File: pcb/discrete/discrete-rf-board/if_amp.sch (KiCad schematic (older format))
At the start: 48 parts, among them Q401 NSVT65011MW6T1G, Q402 Q_NPN_BCE, Q403 NSVT65011MW6T1G, U401 NLAS4157DFT2G, U402 NLAS4157DFT2G, U403 NLAS4157DFT2G, U404 NLAS4157DFT2G

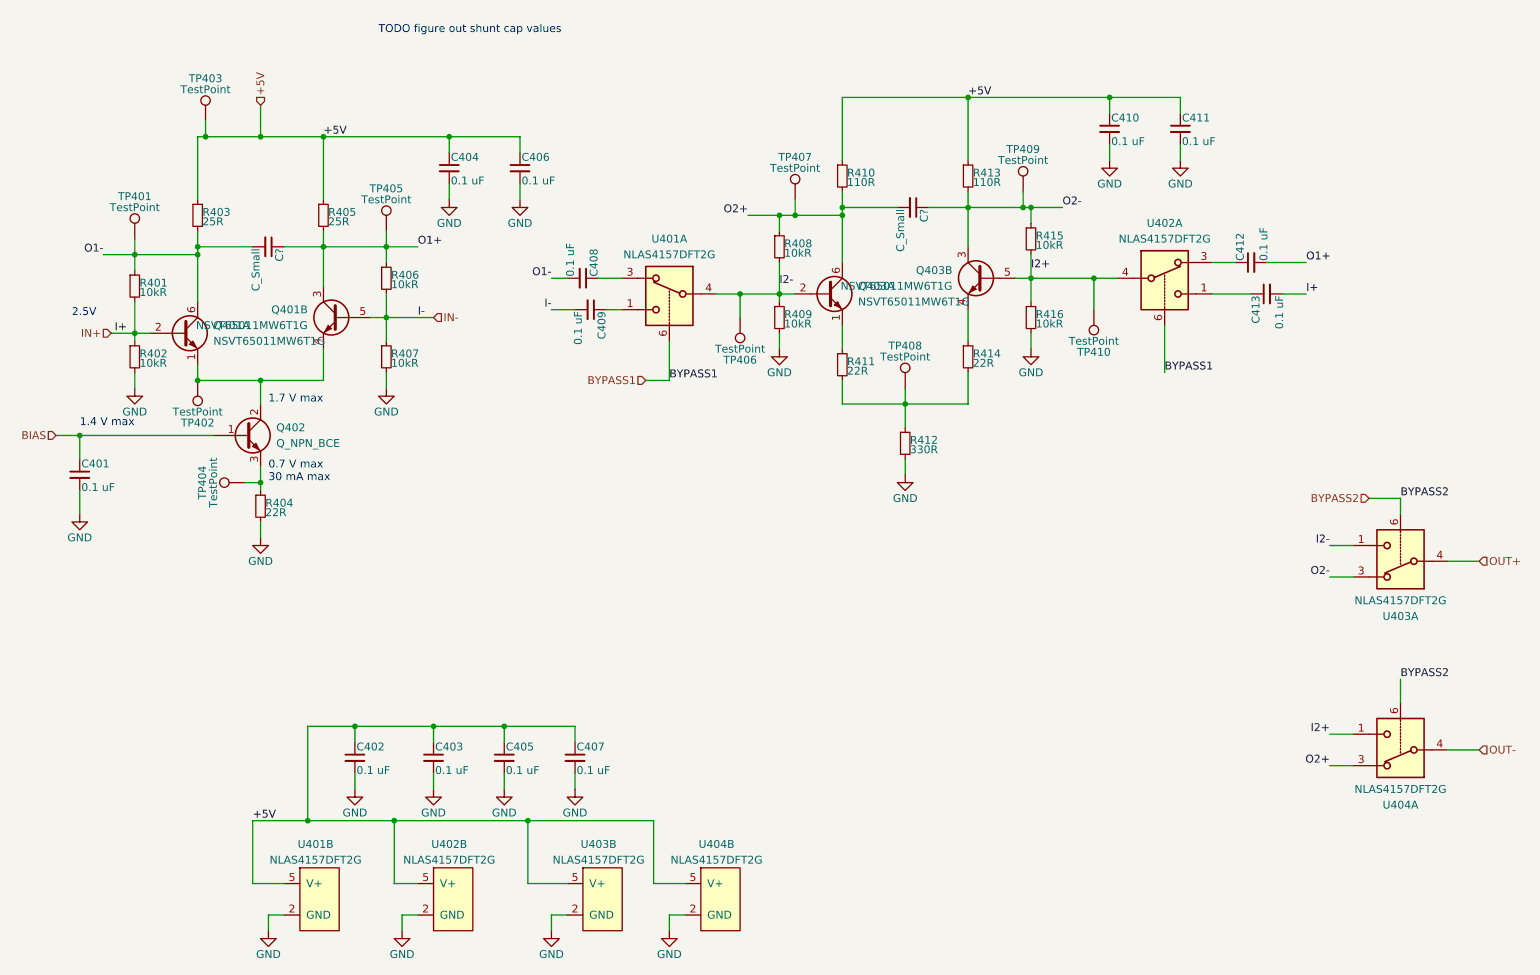
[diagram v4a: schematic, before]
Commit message: Add matching PNP/NPN transistor pairs, fix pin numbering for BFU520R transistors TODO fix biasing on power stage, source last NPN transistor, autofill and start sourcing passives
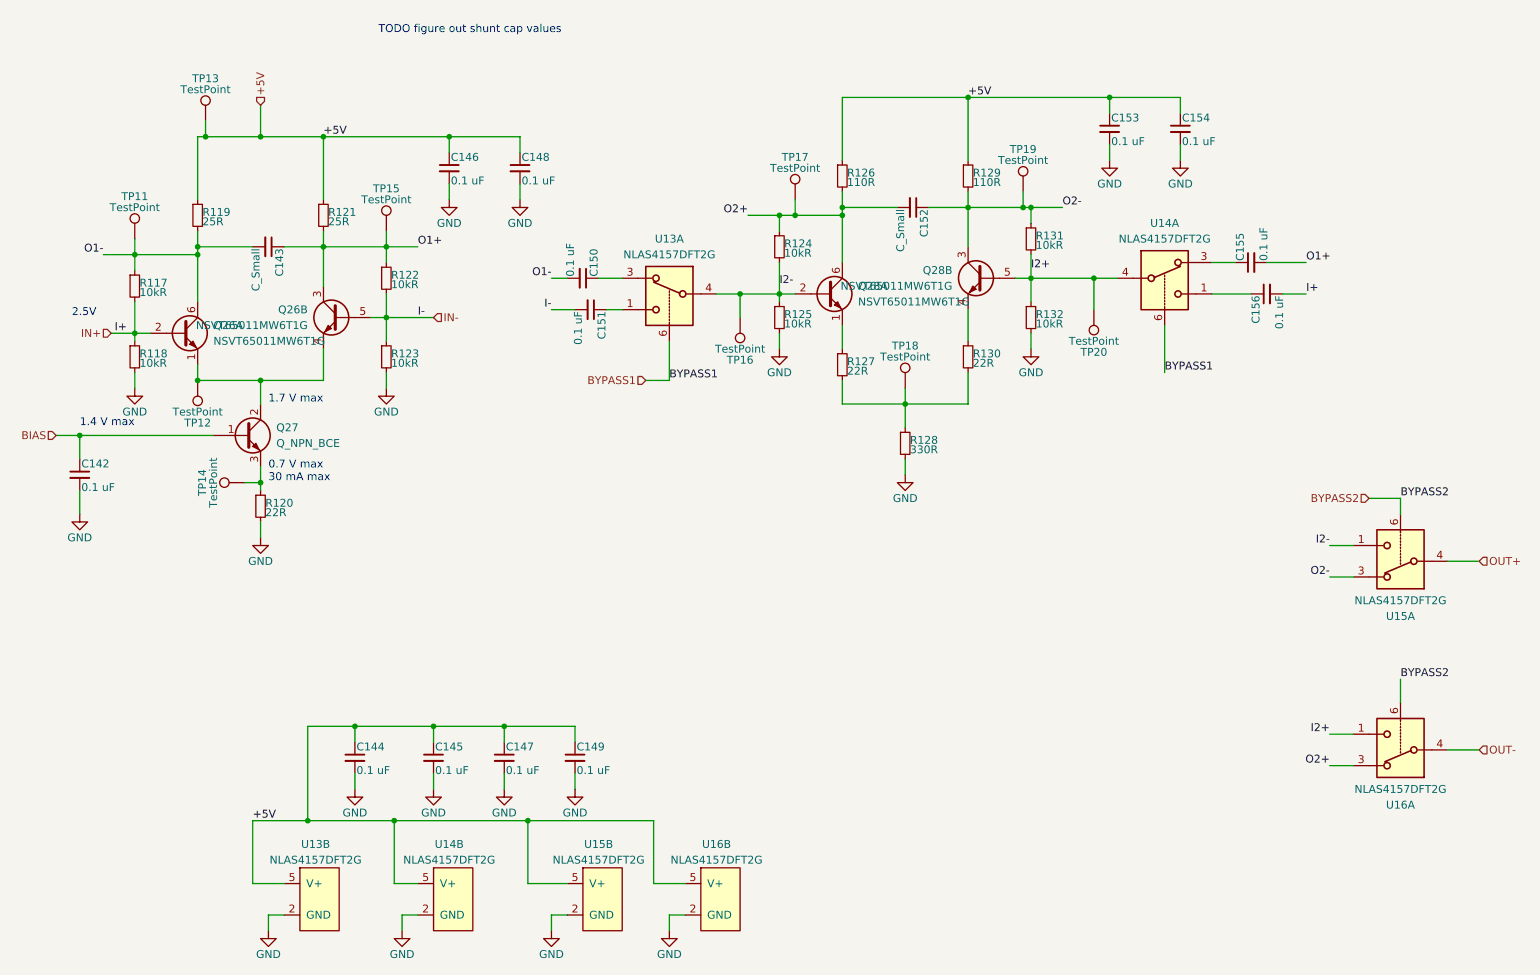
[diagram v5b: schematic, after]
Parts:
- gave numbers to parts that had none: 2
- renumbered C401 to C118, C402 to C120, C403 to C121, C404 to C122, C405 to C123, C406 to C124, C407 to C125, C408 to C126, C409 to C127, C410 to C129, C411 to C130, C412 to C131, C413 to C132, Q401 to Q23, Q402 to Q24, Q403 to Q25, R408 to R100, R409 to R101, R410 to R102, R411 to R103, R412 to R104, R413 to R105, R414 to R106, R415 to R107, R416 to R108, R401 to R93, R402 to R94, R403 to R95, R404 to R96, R405 to R97, R406 to R98, R407 to R99, TP401 to TP1, TP410 to TP10, TP402 to TP2, TP403 to TP3, TP404 to TP4, TP405 to TP5, TP406 to TP6, TP407 to TP7, TP408 to TP8, TP409 to TP9, U403 to U10, U404 to U11, U401 to U8, U402 to U9

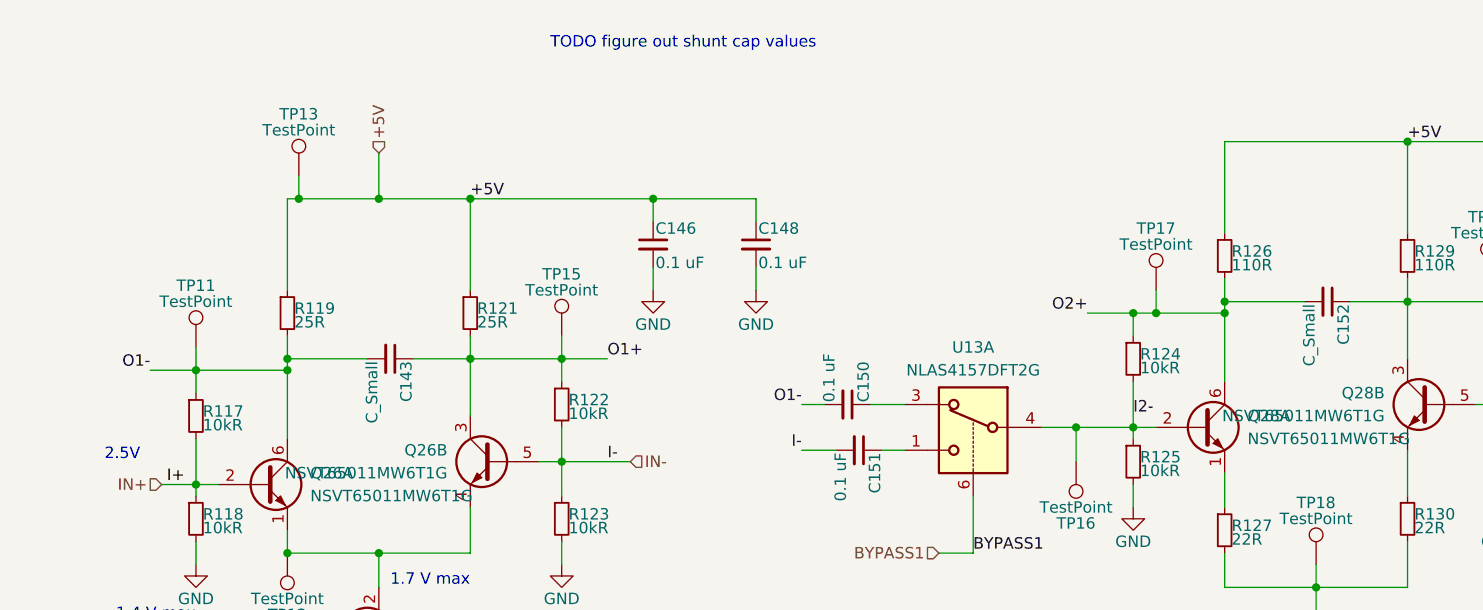
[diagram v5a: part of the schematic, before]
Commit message: All component values set (TODO change transistor gain stages to match values from experimentation
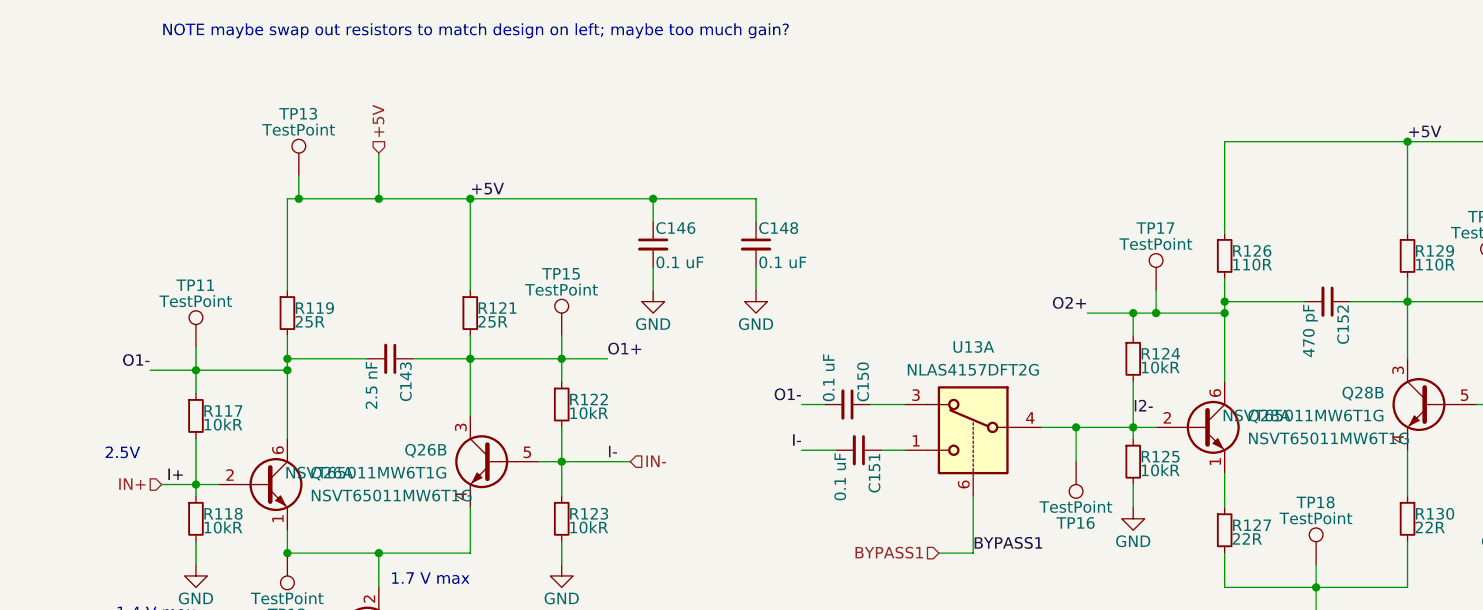
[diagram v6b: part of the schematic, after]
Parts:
- C119: value C_Small -> 2.5 nF
- C128: value C_Small -> 470 pF
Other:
- note added: "NOTE maybe swap out resistors to match design on left; maybe too much gain?"
- note removed: "TODO figure out shunt cap values"
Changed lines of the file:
@@
 $Descr A4 11693 8268
 encoding utf-8
-Sheet 10 19
+Sheet 12 19
 Title ""
 Date ""
@@
 Comment4 ""
 $EndDescr
-$Comp
-L Device:R_Small R95
-U 1 1 5CC4F475
-P 2050 2250
-AR Path="/5CA6B0AA/5CC4DFC2/5CC4F475" Ref="R95"  Part="1"
-AR Path="/5CA6B0AA/5CC9409A/5CC4F475" Ref="R119"  Part="1"
-F 0 "R119" H 2080 2270 50  0000 L CNN
-F 1 "25R" H 2080 2210 50  0000 L CNN
-F 2 "" H 2050 2250 50  0001 C CNN
-F 3 "~" H 2050 2250 50  0001 C CNN
-	1    2050 2250
-	1    0    0    -1
-$EndComp
 $Comp
 L Device:R_Small R97
@@
 AR Path="/5CA6B0AA/5CC9409A/5DA03B3D" Ref="C143"  Part="1"
 F 0 "C143" H 2510 2520 50  0000 L CNN
-F 1 "C_Small" H 2510 2370 50  0000 L CNN
+F 1 "2.5 nF" H 2510 2370 50  0000 L CNN
 F 2 "" H 2500 2450 50  0001 C CNN
 F 3 "~" H 2500 2450 50  0001 C CNN
@@
 AR Path="/5CA6B0AA/5CC9409A/5DA0FE44" Ref="C152"  Part="1"
 F 0 "C152" H 6610 2270 50  0000 L CNN
-F 1 "C_Small" H 6610 2120 50  0000 L CNN
+F 1 "470 pF" H 6610 2120 50  0000 L CNN
 F 2 "" H 6600 2200 50  0001 C CNN
 F 3 "~" H 6600 2200 50  0001 C CNN
@@
 Text Notes 2500 3950 0    50   ~ 0
 0.7 V max\n30 mA max
-Text Notes 3200 1100 0    50   ~ 0
-TODO figure out shunt cap values
+$Comp
+L Device:R_Small R95
+U 1 1 5CC4F475
+P 2050 2250
+AR Path="/5CA6B0AA/5CC4DFC2/5CC4F475" Ref="R95"  Part="1"
+AR Path="/5CA6B0AA/5CC9409A/5CC4F475" Ref="R119"  Part="1"
+F 0 "R119" H 2080 2270 50  0000 L CNN
+F 1 "25R" H 2080 2210 50  0000 L CNN
+F 2 "" H 2050 2250 50  0001 C CNN
+F 3 "~" H 2050 2250 50  0001 C CNN
+	1    2050 2250
+	1    0    0    -1
+$EndComp
+Text Notes 1500 1050 0    50   ~ 0
+NOTE maybe swap out resistors to match design on left; maybe too much gain?
 $EndSCHEMATC

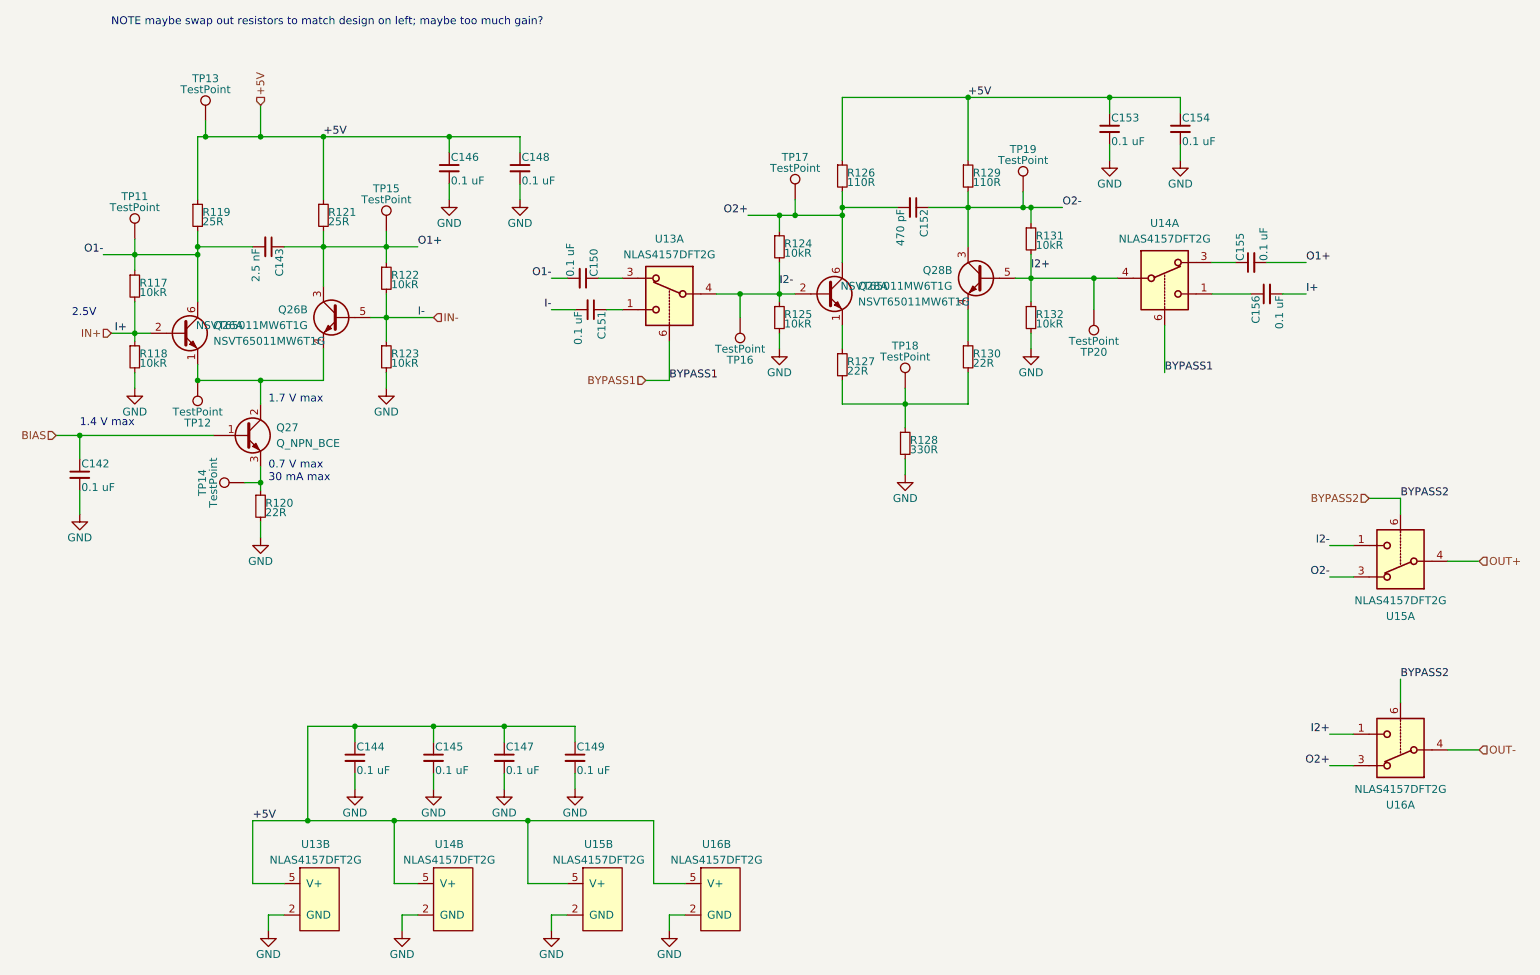
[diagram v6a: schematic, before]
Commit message: Autofill; lots left to do
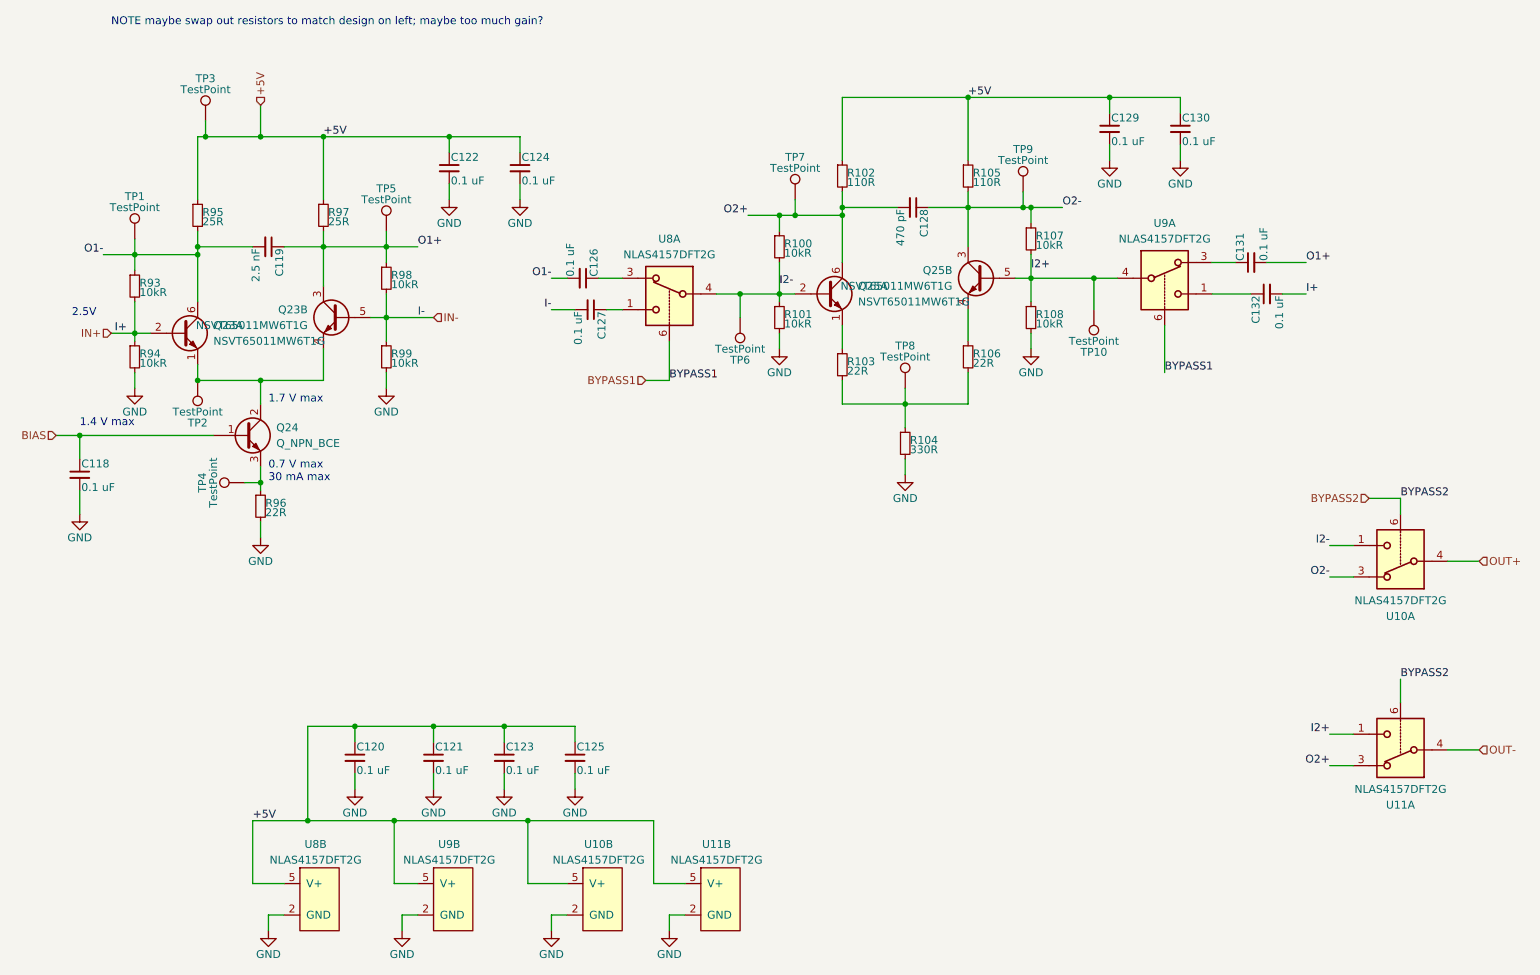
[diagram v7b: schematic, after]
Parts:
- Q23: Mouser (none) -> 863-NSVT65011MW6T1G
- Q25: footprint (none) -> Package_TO_SOT_SMD:SOT-363_SC-70-6_Handsoldering; Mouser (none) -> 863-NSVT65011MW6T1G
- U10, U11, U9: footprint (none) -> Package_TO_SOT_SMD:SOT-363_SC-70-6_Handsoldering
